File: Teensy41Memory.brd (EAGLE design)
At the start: 18.3 x 63.5 mm, 275 parts, among them IC1 25AA080SN, IC2 25AA080SN, IC3 25AA080SN, IC4 25AA080SN, IC5 25AA080SN, IC6 25AA080SN, IC7 25AA080SN, IC8 25AA080SN, IC9 74AC138D

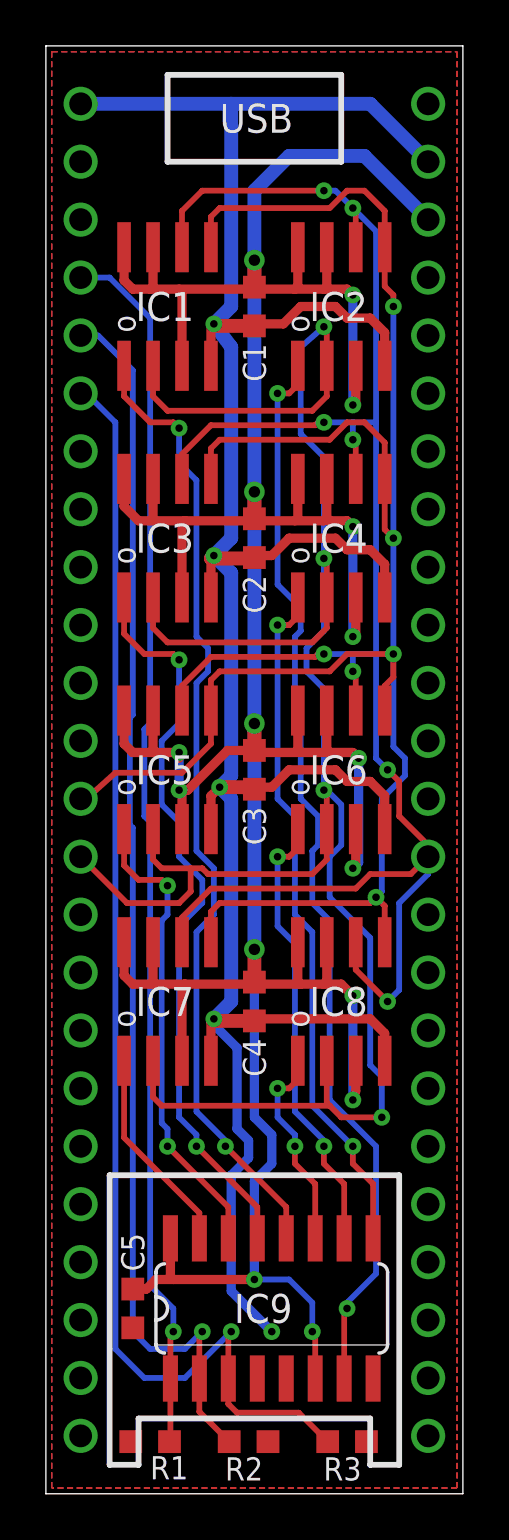
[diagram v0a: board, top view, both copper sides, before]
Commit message: Breakout pin 4 of 74AC138 to disable all CS
It is now possible to set all eight chip selects HIGH on the output of 74AC138 by setting pin4 HIGH. The pin is available on Teensy 4.1 pin 5.
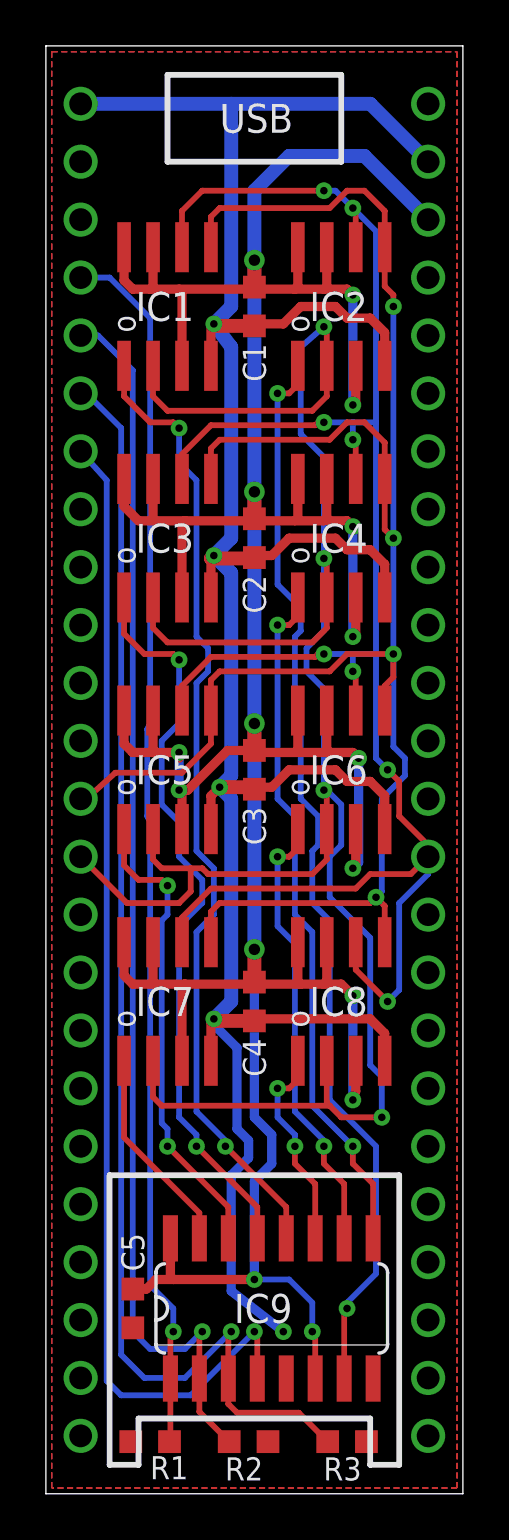
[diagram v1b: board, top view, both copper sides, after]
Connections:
- new net CS3_T: IC9.4
- net DGND: no longer IC9.4
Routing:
- net CS3_T: track 0.00 -> 51.2 mm, vias 0 -> 2
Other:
- board text added: "CS3"
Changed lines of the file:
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@@
 <text x="5.842" y="50.038" size="1.27" layer="26" font="vector" ratio="12" rot="MR0">CS1</text>
 <text x="5.842" y="47.498" size="1.27" layer="26" font="vector" ratio="12" rot="MR0">CS2</text>
+<text x="5.842" y="45.212" size="1.27" layer="26" font="vector" ratio="12" rot="MR0">CS3</text>
 </plain>
 <attributes>
@@
 <wire x1="9.144" y1="20.74" x2="7.454" y2="20.74" width="0.6096" layer="1"/>
 <wire x1="7.454" y1="20.74" x2="7.366" y2="20.828" width="0.6096" layer="1"/>
-<via x="9.906" y="7.112" extent="1-16" drill="0.3302"/>
-<wire x1="9.906" y1="7.112" x2="8.128" y2="8.89" width="0.4064" layer="16"/>
+<via x="10.414" y="7.112" extent="1-16" drill="0.3302"/>
+<wire x1="10.414" y1="7.112" x2="8.128" y2="8.89" width="0.4064" layer="16"/>
 <wire x1="8.128" y1="8.89" x2="8.128" y2="13.97" width="0.4064" layer="16"/>
 <wire x1="8.128" y1="13.97" x2="8.89" y2="14.732" width="0.4064" layer="16"/>
@@
 <wire x1="14.224" y1="51.562" x2="14.859" y2="50.927" width="0.4064" layer="1"/>
 <contactref element="IC9" pad="5"/>
-<contactref element="IC9" pad="4"/>
 <contactref element="R1" pad="1"/>
 <contactref element="R2" pad="1"/>
@@
 <via x="1.524" y="58.42" extent="1-16" drill="1"/>
 <via x="1.524" y="55.88" extent="1-16" drill="1"/>
-<via x="1.524" y="45.72" extent="1-16" drill="1"/>
 <via x="1.524" y="43.18" extent="1-16" drill="1"/>
 <via x="1.524" y="40.64" extent="1-16" drill="1"/>
@@
 <wire x1="1.524" y1="58.42" x2="16.764" y2="60.96" width="0" layer="19" extent="1-1"/>
 <wire x1="1.524" y1="55.88" x2="1.524" y2="58.42" width="0" layer="19" extent="1-1"/>
-<wire x1="1.524" y1="45.72" x2="1.524" y2="55.88" width="0" layer="19" extent="1-1"/>
-<wire x1="1.524" y1="43.18" x2="1.524" y2="45.72" width="0" layer="19" extent="1-1"/>
+<wire x1="1.524" y1="43.18" x2="1.524" y2="55.88" width="0" layer="19" extent="1-1"/>
 <wire x1="1.524" y1="40.64" x2="1.524" y2="43.18" width="0" layer="19" extent="1-1"/>
 <wire x1="1.524" y1="38.1" x2="1.524" y2="40.64" width="0" layer="19" extent="1-1"/>
@@
 <wire x1="2.794" y1="53.34" x2="4.572" y2="51.562" width="0.254" layer="16"/>
 <wire x1="4.572" y1="51.562" x2="4.572" y2="33.782" width="0.254" layer="16"/>
-<wire x1="4.572" y1="33.782" x2="4.318" y2="33.528" width="0.254" layer="16"/>
-<wire x1="4.318" y1="33.528" x2="4.318" y2="29.718" width="0.254" layer="16"/>
-<wire x1="4.318" y1="29.718" x2="4.572" y2="29.464" width="0.254" layer="16"/>
+<wire x1="4.572" y1="33.782" x2="4.445" y2="33.528" width="0.254" layer="16"/>
+<wire x1="4.445" y1="33.528" x2="4.445" y2="29.718" width="0.254" layer="16"/>
+<wire x1="4.445" y1="29.718" x2="4.572" y2="29.464" width="0.254" layer="16"/>
 <wire x1="4.572" y1="29.464" x2="4.572" y2="9.144" width="0.254" layer="16"/>
 <wire x1="4.572" y1="9.144" x2="5.588" y2="8.128" width="0.254" layer="16"/>
@@
 <wire x1="1.524" y1="50.8" x2="2.286" y2="50.8" width="0.254" layer="16"/>
 <wire x1="2.286" y1="50.8" x2="3.81" y2="49.276" width="0.254" layer="16"/>
-<wire x1="3.81" y1="49.276" x2="3.81" y2="34.163" width="0.254" layer="16"/>
-<wire x1="3.81" y1="34.163" x2="3.683" y2="34.036" width="0.254" layer="16"/>
-<wire x1="3.683" y1="34.036" x2="3.683" y2="29.337" width="0.254" layer="16"/>
-<wire x1="3.683" y1="29.337" x2="3.81" y2="29.21" width="0.254" layer="16"/>
-<wire x1="3.81" y1="29.21" x2="3.81" y2="7.112" width="0.254" layer="16"/>
+<wire x1="3.81" y1="49.276" x2="3.81" y2="7.112" width="0.254" layer="16"/>
 <wire x1="3.81" y1="7.112" x2="4.572" y2="6.35" width="0.254" layer="16"/>
 <wire x1="4.572" y1="6.35" x2="6.096" y2="6.35" width="0.254" layer="16"/>
@@
 <contactref element="IC9" pad="3"/>
 <wire x1="1.524" y1="48.26" x2="1.778" y2="48.26" width="0.254" layer="16"/>
-<wire x1="1.778" y1="48.26" x2="3.048" y2="46.99" width="0.254" layer="16"/>
-<wire x1="3.048" y1="46.99" x2="3.048" y2="6.35" width="0.254" layer="16"/>
-<wire x1="3.048" y1="6.35" x2="4.318" y2="5.08" width="0.254" layer="16"/>
+<wire x1="1.778" y1="48.26" x2="3.302" y2="46.736" width="0.254" layer="16"/>
+<wire x1="3.302" y1="46.736" x2="3.302" y2="6.096" width="0.254" layer="16"/>
+<wire x1="3.302" y1="6.096" x2="4.318" y2="5.08" width="0.254" layer="16"/>
 <wire x1="4.318" y1="5.08" x2="6.096" y2="5.08" width="0.254" layer="16"/>
 <wire x1="6.096" y1="5.08" x2="8.128" y2="7.112" width="0.254" layer="16"/>
@@
 <wire x1="11.088" y1="3.556" x2="12.358" y2="2.286" width="0.254" layer="1"/>
 </signal>
+<signal name="CS3_T">
+<contactref element="IC9" pad="4"/>
+<via x="1.524" y="45.72" extent="1-16" drill="1"/>
+<wire x1="1.524" y1="45.72" x2="2.667" y2="44.45" width="0.254" layer="16"/>
+<wire x1="2.667" y1="44.45" x2="2.667" y2="4.953" width="0.254" layer="16"/>
+<wire x1="2.667" y1="4.953" x2="3.302" y2="4.318" width="0.254" layer="16"/>
+<wire x1="3.302" y1="4.318" x2="6.35" y2="4.318" width="0.254" layer="16"/>
+<wire x1="6.35" y1="4.318" x2="9.144" y2="7.112" width="0.254" layer="16"/>
+<via x="9.144" y="7.112" extent="1-16" drill="0.3302"/>
+<wire x1="9.271" y1="5.0546" x2="9.271" y2="6.985" width="0.254" layer="1"/>
+<wire x1="9.271" y1="6.985" x2="9.144" y2="7.112" width="0.254" layer="1"/>
+</signal>
 </signals>
